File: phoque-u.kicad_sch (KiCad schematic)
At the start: 50 parts, among them J1 18…56 V, J2 On / Off, J3 3.3…24 V, Q1 SiR120DP, Q2 SiR120DP, Q3 SiR120DP, Q4 SiR120DP, SW1 Remote, SW2 Voltage select, T1 320 µ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

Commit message: Add dedicated signal and ground layers
This reduces the board dimensions considerably.
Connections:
- net On/Off: now also SW1.1 (A); no longer SW1.2 (B)
- net V_{in}-: now also SW1.2 (B); no longer SW1.1 (A)

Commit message: Widen board for better fit and add mounting holes
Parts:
- added H1, H2, H3, H4: M3, MountingHole:MountingHole_3.2mm_M3_Pad_Via, symbol Mechanical:MountingHole_Pad
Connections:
- net GND: now also H1.1, H2.1, H3.1, H4.1
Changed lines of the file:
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@@
     (pin "2")
+  )
+  (symbol (lib_id "Mechanical:MountingHole_Pad") (at 25.4 153.67 0) (unit 1)
+    (in_bom yes) (on_board yes) (fields_autoplaced)
+    (property "Reference" "H3" (id 0) (at 27.94 151.4915 0)
+      (effects (font (size 1.27 1.27)) (justify left))
+    )
+    (property "Value" "M3" (id 1) (at 27.94 154.2666 0)
+      (effects (font (size 1.27 1.27)) (justify left))
+    )
+    (property "Footprint" "MountingHole:MountingHole_3.2mm_M3_Pad_Via" (id 2) (at 25.4 153.67 0)
+      (effects (font (size 1.27 1.27)) hide)
+    )
+    (property "Datasheet" "~" (id 3) (at 25.4 153.67 0)
+      (effects (font (size 1.27 1.27)) hide)
+    )
+    (pin "1")
+  )
+  (symbol (lib_id "power:GND") (at 273.05 156.21 0) (unit 1)
+    (in_bom yes) (on_board yes) (fields_autoplaced)
+    (property "Reference" "#PWR0101" (id 0) (at 273.05 162.56 0)
+      (effects (font (size 1.27 1.27)) hide)
+    )
+    (property "Value" "GND" (id 1) (at 273.05 160.7725 0))
+    (property "Footprint" "" (id 2) (at 273.05 156.21 0)
+      (effects (font (size 1.27 1.27)) hide)
+    )
+    (property "Datasheet" "" (id 3) (at 273.05 156.21 0)
+      (effects (font (size 1.27 1.27)) hide)
+    )
+    (pin "1")
   )
   (symbol (lib_id "Local:SiR120DP") (at 105.41 64.77 270) (mirror x) (unit 1)
@@
     (pin "4")
     (pin "5")
+  )
+  (symbol (lib_id "power:GND") (at 25.4 29.21 0) (unit 1)
+    (in_bom yes) (on_board yes) (fields_autoplaced)
+    (property "Reference" "#PWR0102" (id 0) (at 25.4 35.56 0)
+      (effects (font (size 1.27 1.27)) hide)
+    )
+    (property "Value" "GND" (id 1) (at 25.4 33.7725 0))
+    (property "Footprint" "" (id 2) (at 25.4 29.21 0)
+      (effects (font (size 1.27 1.27)) hide)
+    )
+    (property "Datasheet" "" (id 3) (at 25.4 29.21 0)
+      (effects (font (size 1.27 1.27)) hide)
+    )
+    (pin "1")
+  )
+  (symbol (lib_id "Mechanical:MountingHole_Pad") (at 273.05 153.67 0) (unit 1)
+    (in_bom yes) (on_board yes) (fields_autoplaced)
+    (property "Reference" "H4" (id 0) (at 275.59 151.4915 0)
+      (effects (font (size 1.27 1.27)) (justify left))
+    )
+    (property "Value" "M3" (id 1) (at 275.59 154.2666 0)
+      (effects (font (size 1.27 1.27)) (justify left))
+    )
+    (property "Footprint" "MountingHole:MountingHole_3.2mm_M3_Pad_Via" (id 2) (at 273.05 153.67 0)
+      (effects (font (size 1.27 1.27)) hide)
+    )
+    (property "Datasheet" "~" (id 3) (at 273.05 153.67 0)
+      (effects (font (size 1.27 1.27)) hide)
+    )
+    (pin "1")
   )
   (symbol (lib_id "Switch:SW_DIP_x12") (at 198.12 110.49 90) (unit 1)
@@
     (pin "5")
   )
+  (symbol (lib_id "power:GND") (at 25.4 156.21 0) (unit 1)
+    (in_bom yes) (on_board yes) (fields_autoplaced)
+    (property "Reference" "#PWR0104" (id 0) (at 25.4 162.56 0)
+      (effects (font (size 1.27 1.27)) hide)
+    )
+    (property "Value" "GND" (id 1) (at 25.4 160.7725 0))
+    (property "Footprint" "" (id 2) (at 25.4 156.21 0)
+      (effects (font (size 1.27 1.27)) hide)
+    )
+    (property "Datasheet" "" (id 3) (at 25.4 156.21 0)
+      (effects (font (size 1.27 1.27)) hide)
+    )
+    (pin "1")
+  )
   (symbol (lib_id "Device:C_Polarized_Small") (at 135.89 76.2 0) (mirror y) (unit 1)
     (in_bom yes) (on_board yes)
@@
     (pin "1")
     (pin "2")
+  )
+  (symbol (lib_id "Mechanical:MountingHole_Pad") (at 25.4 26.67 0) (unit 1)
+    (in_bom yes) (on_board yes) (fields_autoplaced)
+    (property "Reference" "H1" (id 0) (at 27.94 24.4915 0)
+      (effects (font (size 1.27 1.27)) (justify left))
+    )
+    (property "Value" "M3" (id 1) (at 27.94 27.2666 0)
+      (effects (font (size 1.27 1.27)) (justify left))
+    )
+    (property "Footprint" "MountingHole:MountingHole_3.2mm_M3_Pad_Via" (id 2) (at 25.4 26.67 0)
+      (effects (font (size 1.27 1.27)) hide)
+    )
+    (property "Datasheet" "~" (id 3) (at 25.4 26.67 0)
+      (effects (font (size 1.27 1.27)) hide)
+    )
+    (pin "1")
   )
   (symbol (lib_id "Device:Fuse") (at 34.29 86.36 90) (mirror x) (unit 1)
@@
     (pin "2")
   )
+  (symbol (lib_id "power:GND") (at 273.05 29.21 0) (unit 1)
+    (in_bom yes) (on_board yes) (fields_autoplaced)
+    (property "Reference" "#PWR0103" (id 0) (at 273.05 35.56 0)
+      (effects (font (size 1.27 1.27)) hide)
+    )
+    (property "Value" "GND" (id 1) (at 273.05 33.7725 0))
+    (property "Footprint" "" (id 2) (at 273.05 29.21 0)
+      (effects (font (size 1.27 1.27)) hide)
+    )
+    (property "Datasheet" "" (id 3) (at 273.05 29.21 0)
+      (effects (font (size 1.27 1.27)) hide)
+    )
+    (pin "1")
+  )
   (symbol (lib_id "Local:SiR120DP") (at 123.19 96.52 90) (mirror x) (unit 1)
     (in_bom yes) (on_board yes) (fields_autoplaced)
@@
     (pin "4")
     (pin "5")
+  )
+  (symbol (lib_id "Mechanical:MountingHole_Pad") (at 273.05 26.67 0) (unit 1)
+    (in_bom yes) (on_board yes) (fields_autoplaced)
+    (property "Reference" "H2" (id 0) (at 275.59 24.4915 0)
+      (effects (font (size 1.27 1.27)) (justify left))
+    )
+    (property "Value" "M3" (id 1) (at 275.59 27.2666 0)
+      (effects (font (size 1.27 1.27)) (justify left))
+    )
+    (property "Footprint" "MountingHole:MountingHole_3.2mm_M3_Pad_Via" (id 2) (at 273.05 26.67 0)
+      (effects (font (size 1.27 1.27)) hide)
+    )
+    (property "Datasheet" "~" (id 3) (at 273.05 26.67 0)
+      (effects (font (size 1.27 1.27)) hide)
+    )
+    (pin "1")
   )
   (symbol (lib_id "Local:LT4320") (at 114.3 76.2 0) (unit 1)
@@
       (reference "#PWR06") (unit 1) (value "GND") (footprint "")
     )
+    (path "/0d95c66b-b103-4abd-94dd-dcc82ea6e38c"
+      (reference "#PWR0101") (unit 1) (value "GND") (footprint "")
+    )
+    (path "/26e710fa-e187-4e29-9de4-4e8ff64e7115"
+      (reference "#PWR0102") (unit 1) (value "GND") (footprint "")
+    )
+    (path "/b9f54358-990a-4b01-81f0-fe0150e4dc7c"
+      (reference "#PWR0103") (unit 1) (value "GND") (footprint "")
+    )
+    (path "/79a88a0a-c664-45d7-b87f-32c912acda3d"
+      (reference "#PWR0104") (unit 1) (value "GND") (footprint "")
+    )
     (path "/00000000-0000-0000-0000-000061cf0684"
       (reference "C1") (unit 1) (value "4n7") (footprint "Local:C_Disc_D13mm_W6.0mm_P10.00mm")
@@
       (reference "GD2") (unit 1) (value "75 V") (footprint "Local:2036-NN-SM")
     )
+    (path "/835ada2e-dc88-46f5-b472-12f6a1e8c9f4"
+      (reference "H1") (unit 1) (value "M3") (footprint "MountingHole:MountingHole_3.2mm_M3_Pad_Via")
+    )
+    (path "/dfe7aa15-3d3f-4a25-935c-577ae609d381"
+      (reference "H2") (unit 1) (value "M3") (footprint "MountingHole:MountingHole_3.2mm_M3_Pad_Via")
+    )
+    (path "/0862de5e-b5b6-45ca-bb25-3ec987e38f71"
+      (reference "H3") (unit 1) (value "M3") (footprint "MountingHole:MountingHole_3.2mm_M3_Pad_Via")
+    )
+    (path "/34448c9f-5d0d-4bc4-9b86-67e6ab36b8a1"
+      (reference "H4") (unit 1) (value "M3") (footprint "MountingHole:MountingHole_3.2mm_M3_Pad_Via")
+    )
     (path "/00000000-0000-0000-0000-000061ce1fbe"

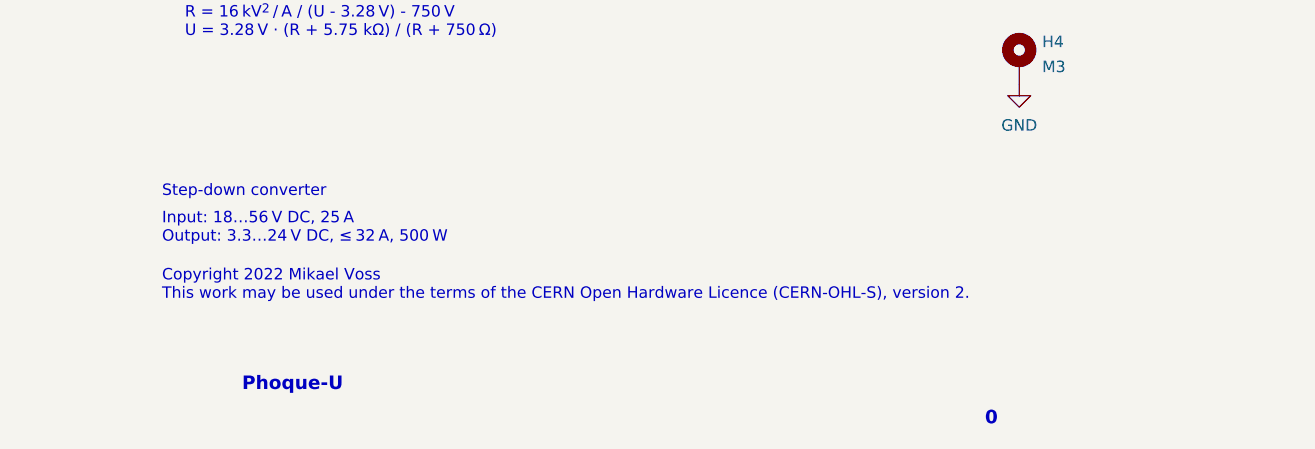
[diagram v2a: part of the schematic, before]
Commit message: Clean up silkscreen
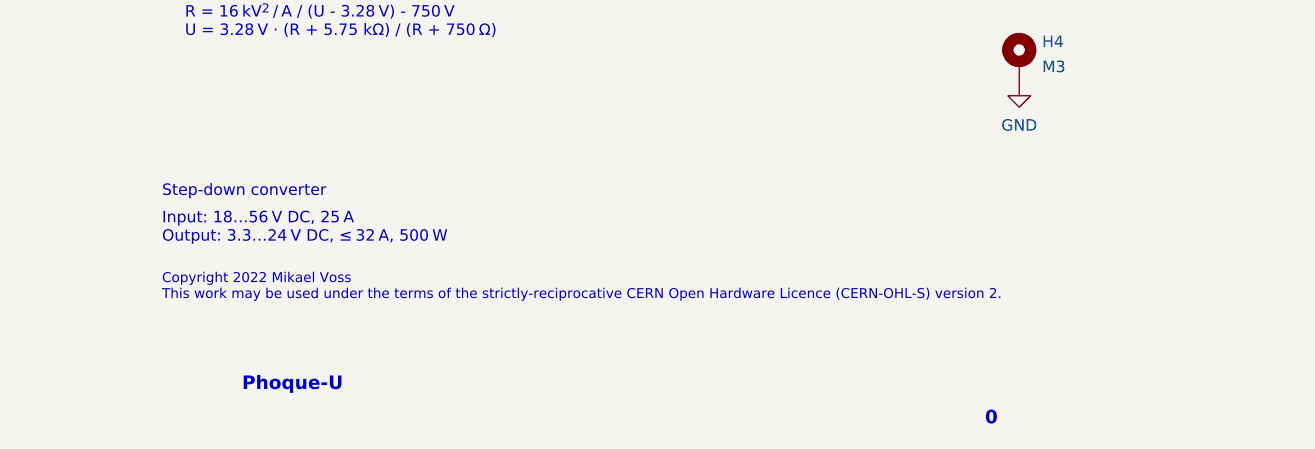
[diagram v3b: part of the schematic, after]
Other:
- note added: "Copyright 2022 Mikael Voss This work may be used under the terms of the strictly‐reciprocative CERN Open Hardware Licence (CERN-OHL-S) version 2."
- note removed: "Copyright 2022 Mikael Voss This work may be used under the terms of the CERN Open Hardware Licence (CERN-OHL-S), version 2."
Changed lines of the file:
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@@
     (effects (font (size 1.27 1.27)) (justify left bottom))
   )
-  (text "Copyright 2022 Mikael Voss\nThis work may be used under the terms of the CERN Open Hardware Licence (CERN-OHL-S), version 2."
+  (text "Copyright 2022 Mikael Voss\nThis work may be used under the terms of the strictly‐reciprocative CERN Open Hardware Licence (CERN-OHL-S) version 2."
     (at 177.8 180.34 0)
-    (effects (font (size 1.27 1.27)) (justify left bottom))
+    (effects (font (size 1.1 1.1)) (justify left bottom))
   )
   (text "Input: 18…56 V DC, 25 A\nOutput: 3.3…24 V DC, ≤ 32 A, 500 W"

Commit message: Clear pads from silkscreen
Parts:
- C11, C5, C6: footprint Capacitor_THT:CP_Radial_D16.0mm_P7.50mm -> Local:CP_Radial_D16.0mm_P7.50mm
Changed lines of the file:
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@@
       (effects (font (size 1.27 1.27)) (justify right))
     )
-    (property "Footprint" "Capacitor_THT:CP_Radial_D16.0mm_P7.50mm" (id 2) (at 191.77 76.2 0)
+    (property "Footprint" "Local:CP_Radial_D16.0mm_P7.50mm" (id 2) (at 191.77 76.2 0)
       (effects (font (size 1.27 1.27)) hide)
     )
@@
       (effects (font (size 1.27 1.27)) (justify left))
     )
-    (property "Footprint" "Capacitor_THT:CP_Radial_D16.0mm_P7.50mm" (id 2) (at 143.51 76.2 0)
+    (property "Footprint" "Local:CP_Radial_D16.0mm_P7.50mm" (id 2) (at 143.51 76.2 0)
       (effects (font (size 1.27 1.27)) hide)
     )
@@
       (effects (font (size 1.27 1.27)) (justify left))
     )
-    (property "Footprint" "Capacitor_THT:CP_Radial_D16.0mm_P7.50mm" (id 2) (at 135.89 76.2 0)
+    (property "Footprint" "Local:CP_Radial_D16.0mm_P7.50mm" (id 2) (at 135.89 76.2 0)
       (effects (font (size 1.27 1.27)) hide)
     )
@@
     )
     (path "/7c052fb9-fecd-48a6-b115-90192e80ae2b"
-      (reference "C5") (unit 1) (value "470 µ") (footprint "Capacitor_THT:CP_Radial_D16.0mm_P7.50mm")
+      (reference "C5") (unit 1) (value "470 µ") (footprint "Local:CP_Radial_D16.0mm_P7.50mm")
     )
     (path "/545dcca5-4516-4b56-930c-fa32800a5d09"
-      (reference "C6") (unit 1) (value "470 µ") (footprint "Capacitor_THT:CP_Radial_D16.0mm_P7.50mm")
+      (reference "C6") (unit 1) (value "470 µ") (footprint "Local:CP_Radial_D16.0mm_P7.50mm")
     )
     (path "/00000000-0000-0000-0000-000061de344a"
@@
     )
     (path "/00000000-0000-0000-0000-000061de7a61"
-      (reference "C11") (unit 1) (value "470 µ") (footprint "Capacitor_THT:CP_Radial_D16.0mm_P7.50mm")
+      (reference "C11") (unit 1) (value "470 µ") (footprint "Local:CP_Radial_D16.0mm_P7.50mm")
     )
     (path "/00000000-0000-0000-0000-000061d6d659"
